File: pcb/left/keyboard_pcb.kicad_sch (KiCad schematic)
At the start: 121 parts, among them U1 Flippable RP2040 ProMicro/nic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

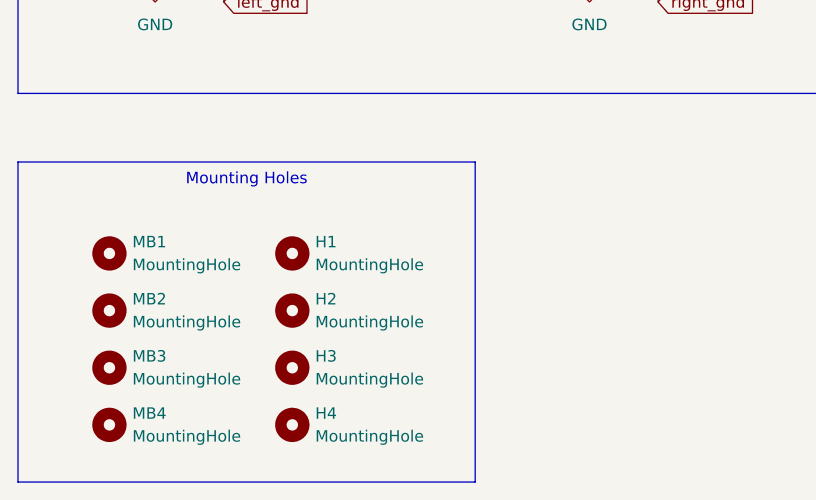
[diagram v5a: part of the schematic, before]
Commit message: Fix mounting holes
There were two H1s and three H4s! Add H5–7 and assign M2 mounting hole from KiCad library (no visible change noticed when updating on PCB).
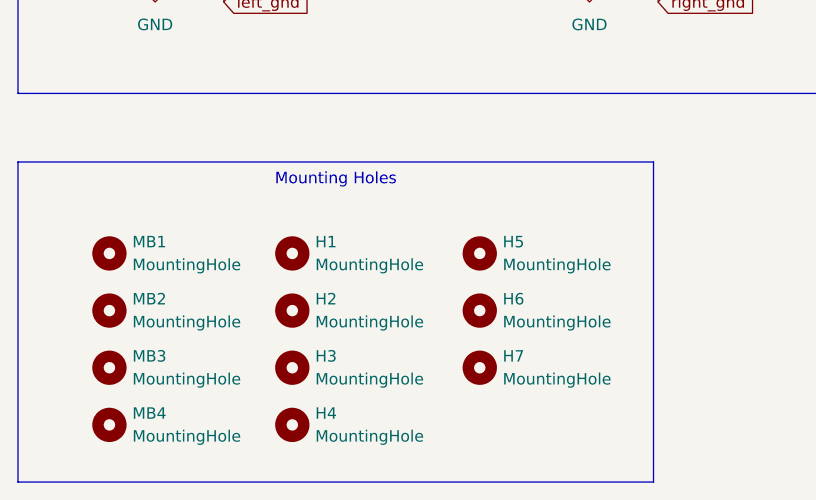
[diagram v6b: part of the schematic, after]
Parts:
- added H5, H6, H7: MountingHole, MountingHole:MountingHole_2.2mm_M2, symbol Mechanical:MountingHole
- H1, H2, H3, H4: footprint beekeeb_lib:MountingHole_2.2mm_M2-8mm -> MountingHole:MountingHole_2.2mm_M2
- 右J2, 左J2: footprint _Project Library:USB_C_Receptacle_GCT_USB4125-xx-x_6P_TopMnt_Horizontal_Flippable -> _Project Library:USB_C_Receptacle_GCT_USB4125-xx-x_6P_TopMnt_Horizontal_Mirrorable
- 右S1, 左S1: footprint _Project Library:SW_MSK12C02-HB_Flippable -> _Project Library:SW_MSK12C02-HB_Mirrorable
- 右S2: footprint _Project Library:USB_C_Receptacle_GCT_USB4125-xx-x_6P_TopMnt_Horizontal_Flippable -> (none)
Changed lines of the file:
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@@
   )
   (text_box "Mounting Holes"
-    (at 17.78 238.76 0) (size 50.8 35.56)
+    (at 17.78 238.76 0) (size 70.612 35.56)
     (stroke (width 0) (type default))
     (fill (type none))
@@
     )
   )
+  (symbol (lib_id "Mechanical:MountingHole") (at 69.088 255.27 0) (unit 1)
+    (in_bom yes) (on_board yes) (dnp no) (fields_autoplaced)
+    (property "Reference" "H6" (at 71.628 253.9999 0)
+      (effects (font (size 1.27 1.27)) (justify left))
+    )
+    (property "Value" "MountingHole" (at 71.628 256.5399 0)
+      (effects (font (size 1.27 1.27)) (justify left))
+    )
+    (property "Footprint" "MountingHole:MountingHole_2.2mm_M2" (at 69.088 255.27 0)
+      (effects (font (size 1.27 1.27)) hide)
+    )
+    (property "Datasheet" "~" (at 69.088 255.27 0)
+      (effects (font (size 1.27 1.27)) hide)
+    )
+    (instances
+      (project "keyboard_pcb"
+        (path "/9538e4ed-27e6-4c37-b989-9859dc0d49e8"
+          (reference "H6") (unit 1)
+        )
+      )
+    )
+  )
   (symbol (lib_id "Device:D") (at 269.24 229.87 90) (unit 1)
     (in_bom yes) (on_board yes) (dnp no) (fields_autoplaced)
@@
       (effects (font (size 1.27 1.27)) (justify left))
     )
-    (property "Footprint" "beekeeb_lib:MountingHole_2.2mm_M2-8mm" (at 48.26 267.97 0)
+    (property "Footprint" "MountingHole:MountingHole_2.2mm_M2" (at 48.26 267.97 0)
       (effects (font (size 1.27 1.27)) hide)
     )
@@
     )
   )
+  (symbol (lib_id "Mechanical:MountingHole") (at 69.088 261.62 0) (unit 1)
+    (in_bom yes) (on_board yes) (dnp no) (fields_autoplaced)
+    (property "Reference" "H7" (at 71.628 260.3499 0)
+      (effects (font (size 1.27 1.27)) (justify left))
+    )
+    (property "Value" "MountingHole" (at 71.628 262.8899 0)
+      (effects (font (size 1.27 1.27)) (justify left))
+    )
+    (property "Footprint" "MountingHole:MountingHole_2.2mm_M2" (at 69.088 261.62 0)
+      (effects (font (size 1.27 1.27)) hide)
+    )
+    (property "Datasheet" "~" (at 69.088 261.62 0)
+      (effects (font (size 1.27 1.27)) hide)
+    )
+    (instances
+      (project "keyboard_pcb"
+        (path "/9538e4ed-27e6-4c37-b989-9859dc0d49e8"
+          (reference "H7") (unit 1)
+        )
+      )
+    )
+  )
   (symbol (lib_id "Device:D") (at 223.52 176.53 90) (unit 1)
     (in_bom yes) (on_board yes) (dnp no) (fields_autoplaced)
@@
       (effects (font (size 1.27 1.27)) (justify left))
     )
-    (property "Footprint" "beekeeb_lib:MountingHole_2.2mm_M2-8mm" (at 48.26 255.27 0)
+    (property "Footprint" "MountingHole:MountingHole_2.2mm_M2" (at 48.26 255.27 0)
       (effects (font (size 1.27 1.27)) hide)
     )
@@
     )
   )
+  (symbol (lib_id "Mechanical:MountingHole") (at 69.088 248.92 0) (unit 1)
+    (in_bom yes) (on_board yes) (dnp no) (fields_autoplaced)
+    (property "Reference" "H5" (at 71.628 247.6499 0)
+      (effects (font (size 1.27 1.27)) (justify left))
+    )
+    (property "Value" "MountingHole" (at 71.628 250.1899 0)
+      (effects (font (size 1.27 1.27)) (justify left))
+    )
+    (property "Footprint" "MountingHole:MountingHole_2.2mm_M2" (at 69.088 248.92 0)
+      (effects (font (size 1.27 1.27)) hide)
+    )
+    (property "Datasheet" "~" (at 69.088 248.92 0)
+      (effects (font (size 1.27 1.27)) hide)
+    )
+    (instances
+      (project "keyboard_pcb"
+        (path "/9538e4ed-27e6-4c37-b989-9859dc0d49e8"
+          (reference "H5") (unit 1)
+        )
+      )
+    )
+  )
   (symbol (lib_id "Device:D") (at 190.5 250.19 90) (unit 1)
     (in_bom yes) (on_board yes) (dnp no)
@@
       (effects (font (size 1.27 1.27)))
     )
-    (property "Footprint" "_Project Library:SW_MSK12C02-HB_Flippable" (at 48.26 114.3 0)
+    (property "Footprint" "_Project Library:SW_MSK12C02-HB_Mirrorable" (at 48.26 114.3 0)
       (effects (font (size 1.27 1.27)) hide)
     )
@@
       (effects (font (size 1.27 1.27)))
     )
-    (property "Footprint" "_Project Library:SW_MSK12C02-HB_Flippable" (at 48.26 101.6 0)
+    (property "Footprint" "_Project Library:SW_MSK12C02-HB_Mirrorable" (at 48.26 101.6 0)
       (effects (font (size 1.27 1.27)) hide)
     )
@@
       (effects (font (size 1.27 1.27)))
     )
-    (property "Footprint" "_Project Library:USB_C_Receptacle_GCT_USB4125-xx-x_6P_TopMnt_Horizontal_Flippable" (at 92.71 198.12 0)
+    (property "Footprint" "_Project Library:USB_C_Receptacle_GCT_USB4125-xx-x_6P_TopMnt_Horizontal_Mirrorable" (at 92.71 198.12 0)
       (effects (font (size 1.27 1.27)) hide)
     )
@@
       (effects (font (size 1.27 1.27)) (justify left))
     )
-    (property "Footprint" "beekeeb_lib:MountingHole_2.2mm_M2-8mm" (at 48.26 261.62 0)
+    (property "Footprint" "MountingHole:MountingHole_2.2mm_M2" (at 48.26 261.62 0)
       (effects (font (size 1.27 1.27)) hide)
     )
@@
       (effects (font (size 1.27 1.27)))
     )
-    (property "Footprint" "_Project Library:USB_C_Receptacle_GCT_USB4125-xx-x_6P_TopMnt_Horizontal_Flippable" (at 44.45 198.12 0)
+    (property "Footprint" "_Project Library:USB_C_Receptacle_GCT_USB4125-xx-x_6P_TopMnt_Horizontal_Mirrorable" (at 44.45 198.12 0)
       (effects (font (size 1.27 1.27)) hide)
     )
@@
       (effects (font (size 1.27 1.27)) (justify left))
     )
-    (property "Footprint" "beekeeb_lib:MountingHole_2.2mm_M2-8mm" (at 48.26 248.92 0)
+    (property "Footprint" "MountingHole:MountingHole_2.2mm_M2" (at 48.26 248.92 0)
       (effects (font (size 1.27 1.27)) hide)
     )
@@
       (effects (font (size 1.27 1.27)))
     )
-    (property "Footprint" "_Project Library:USB_C_Receptacle_GCT_USB4125-xx-x_6P_TopMnt_Horizontal_Flippable" (at 45.72 152.4 0)
+    (property "Footprint" "" (at 45.72 152.4 0)
       (effects (font (size 1.27 1.27)) hide)
     )

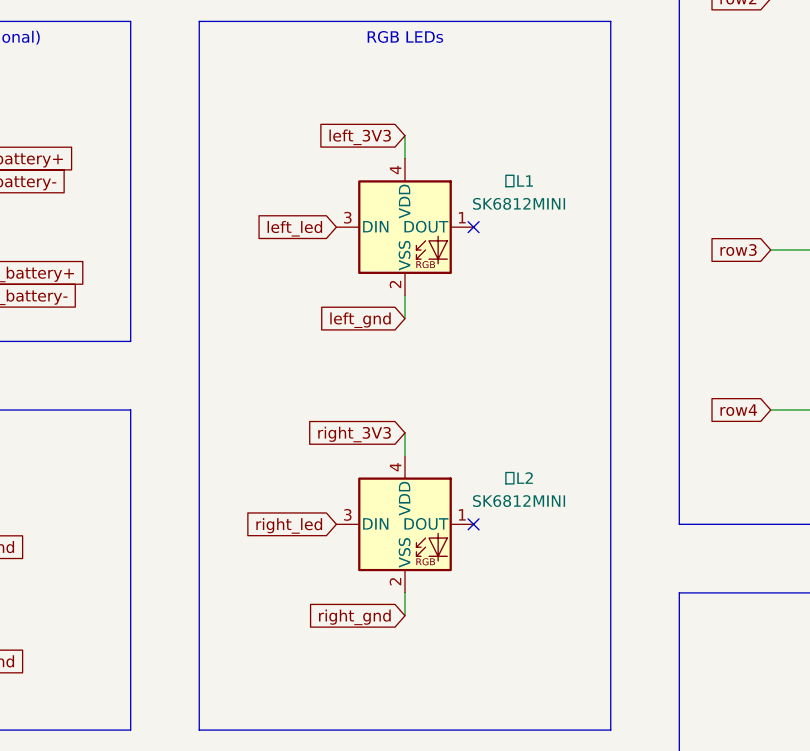
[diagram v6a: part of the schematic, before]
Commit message: Fix pin numbering for SK6812MINI-E
The “E” has a different [pinout](https://cdn-shop.adafruit.com/product-files/4960/4960_SK6812MINI-E_REV02_EN.pdf) to the non-“E”
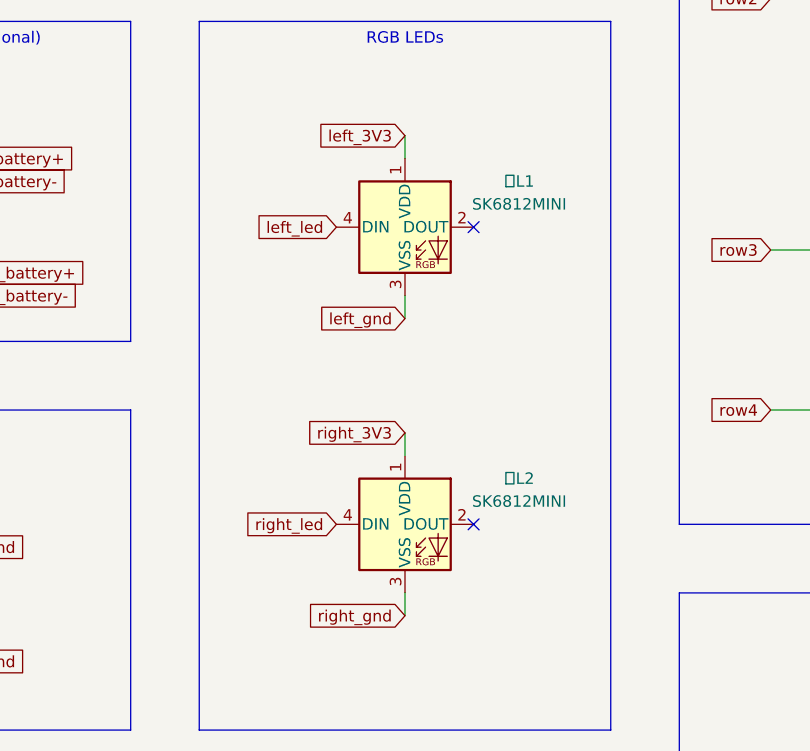
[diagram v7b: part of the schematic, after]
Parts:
- 右L2, 左L1: symbol LED:SK6812MINI -> _Project Library:SK6812MINI-E
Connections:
- net left_3V3: now also 右L2.3 (VSS), 左L1.1 (VDD); no longer 右L2.2 (VSS), 左L1.4 (VDD)
- net left_gnd: now also 右L2.1 (VDD), 左L1.3 (VSS); no longer 右L2.4 (VDD), 左L1.2 (VSS)
- net left_led: now also 左L1.4 (DIN); no longer 左L1.3 (DIN)
- net right_led: now also 右L2.4 (DIN); no longer 右L2.3 (DIN)
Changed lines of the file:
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@@
     )
   )
-  (symbol (lib_id "LED:SK6812MINI") (at 104.14 142.24 0) (unit 1)
+  (symbol (lib_id "_Project Library:SK6812MINI-E") (at 104.14 142.24 0) (unit 1)
     (in_bom yes) (on_board yes) (dnp no)
     (property "Reference" "右L2" (at 116.84 137.16 0)
@@
     )
   )
-  (symbol (lib_id "LED:SK6812MINI") (at 104.14 109.22 0) (unit 1)
+  (symbol (lib_id "_Project Library:SK6812MINI-E") (at 104.14 109.22 0) (unit 1)
     (in_bom yes) (on_board yes) (dnp no)
     (property "Reference" "左L1" (at 116.84 104.14 0)

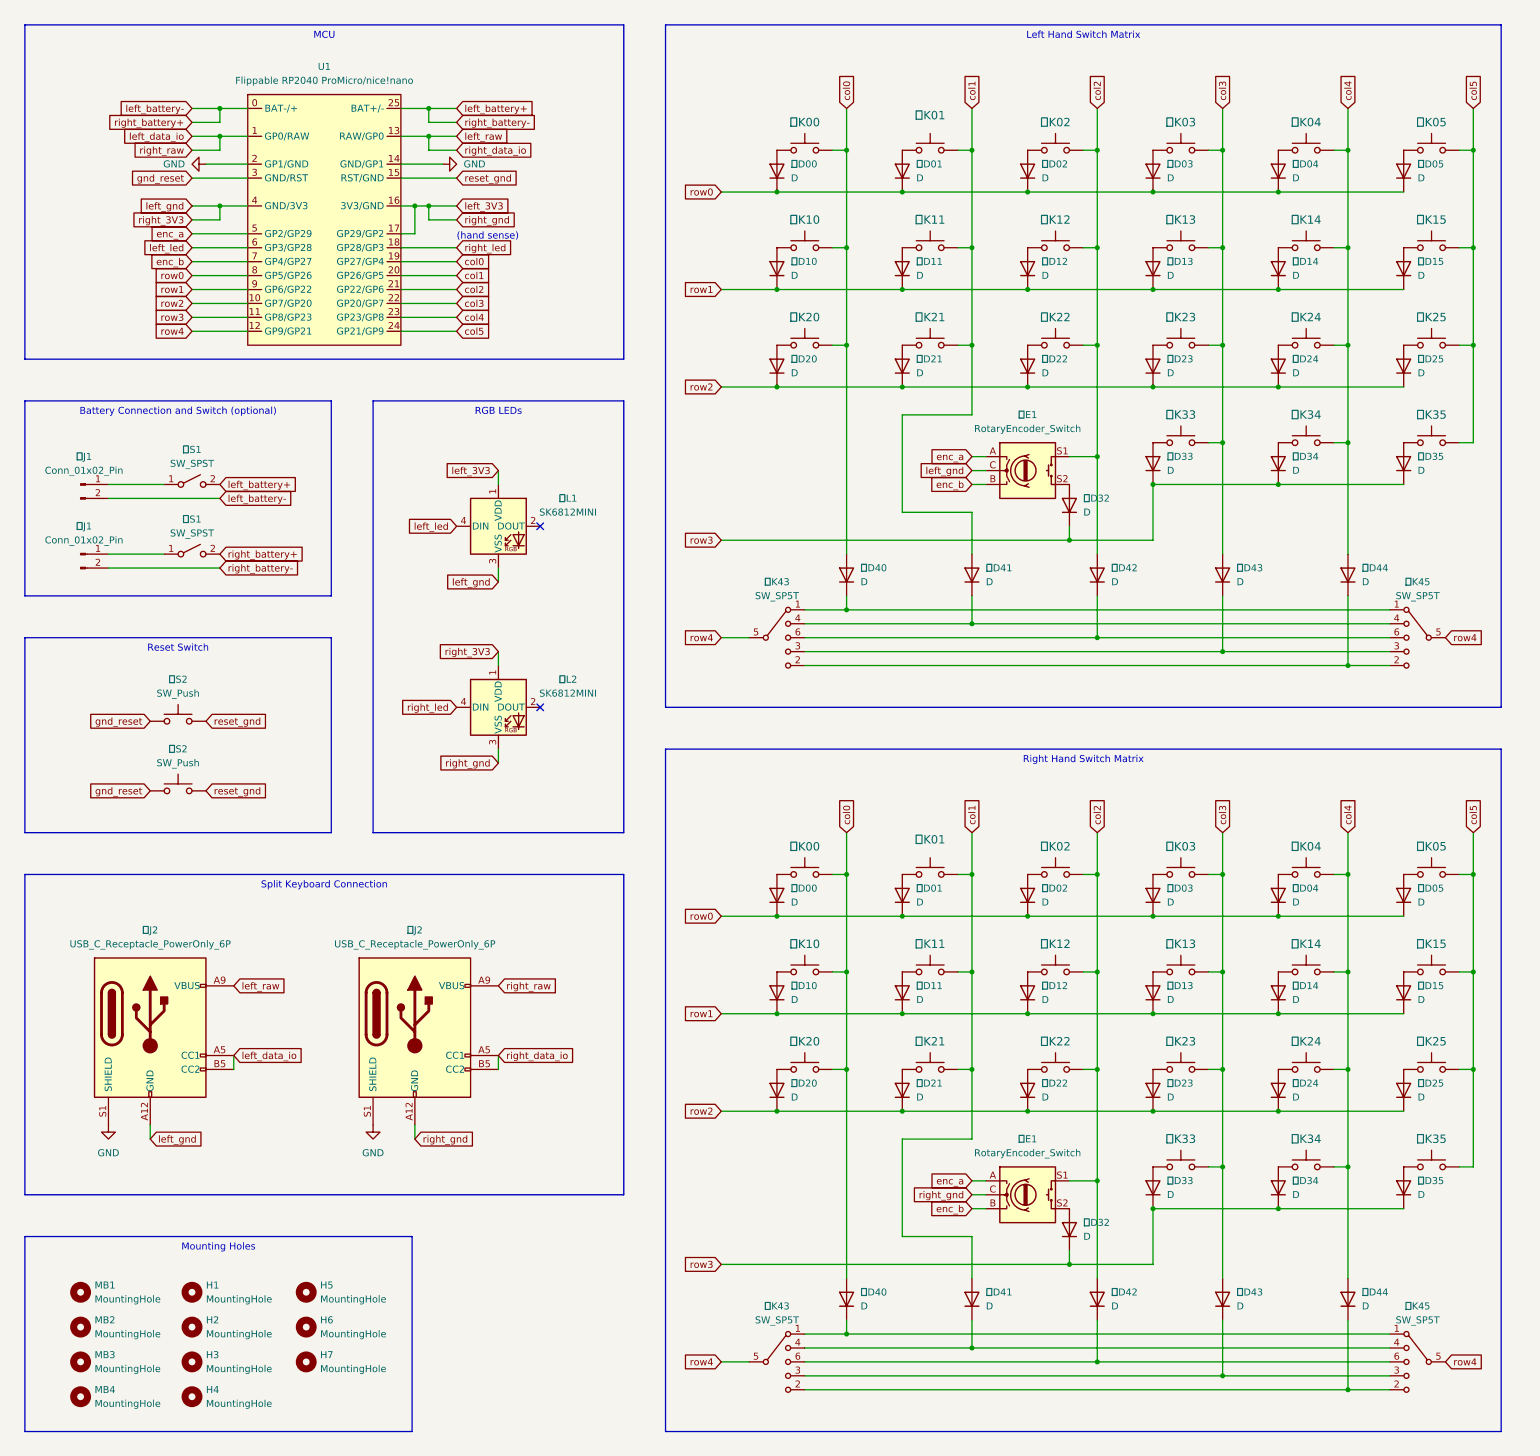
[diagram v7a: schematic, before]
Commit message: Tweak schematic
 * Change power switches to SP**D**T to match MSK12C02
 * Switch from double-named nets to single name that covers both orientations
 * Update flippable ProMicro symbol to remove gaps between pins that are no longer needed
 * Wire connection to ground through SK6812 GND leg, which will act as a jumper
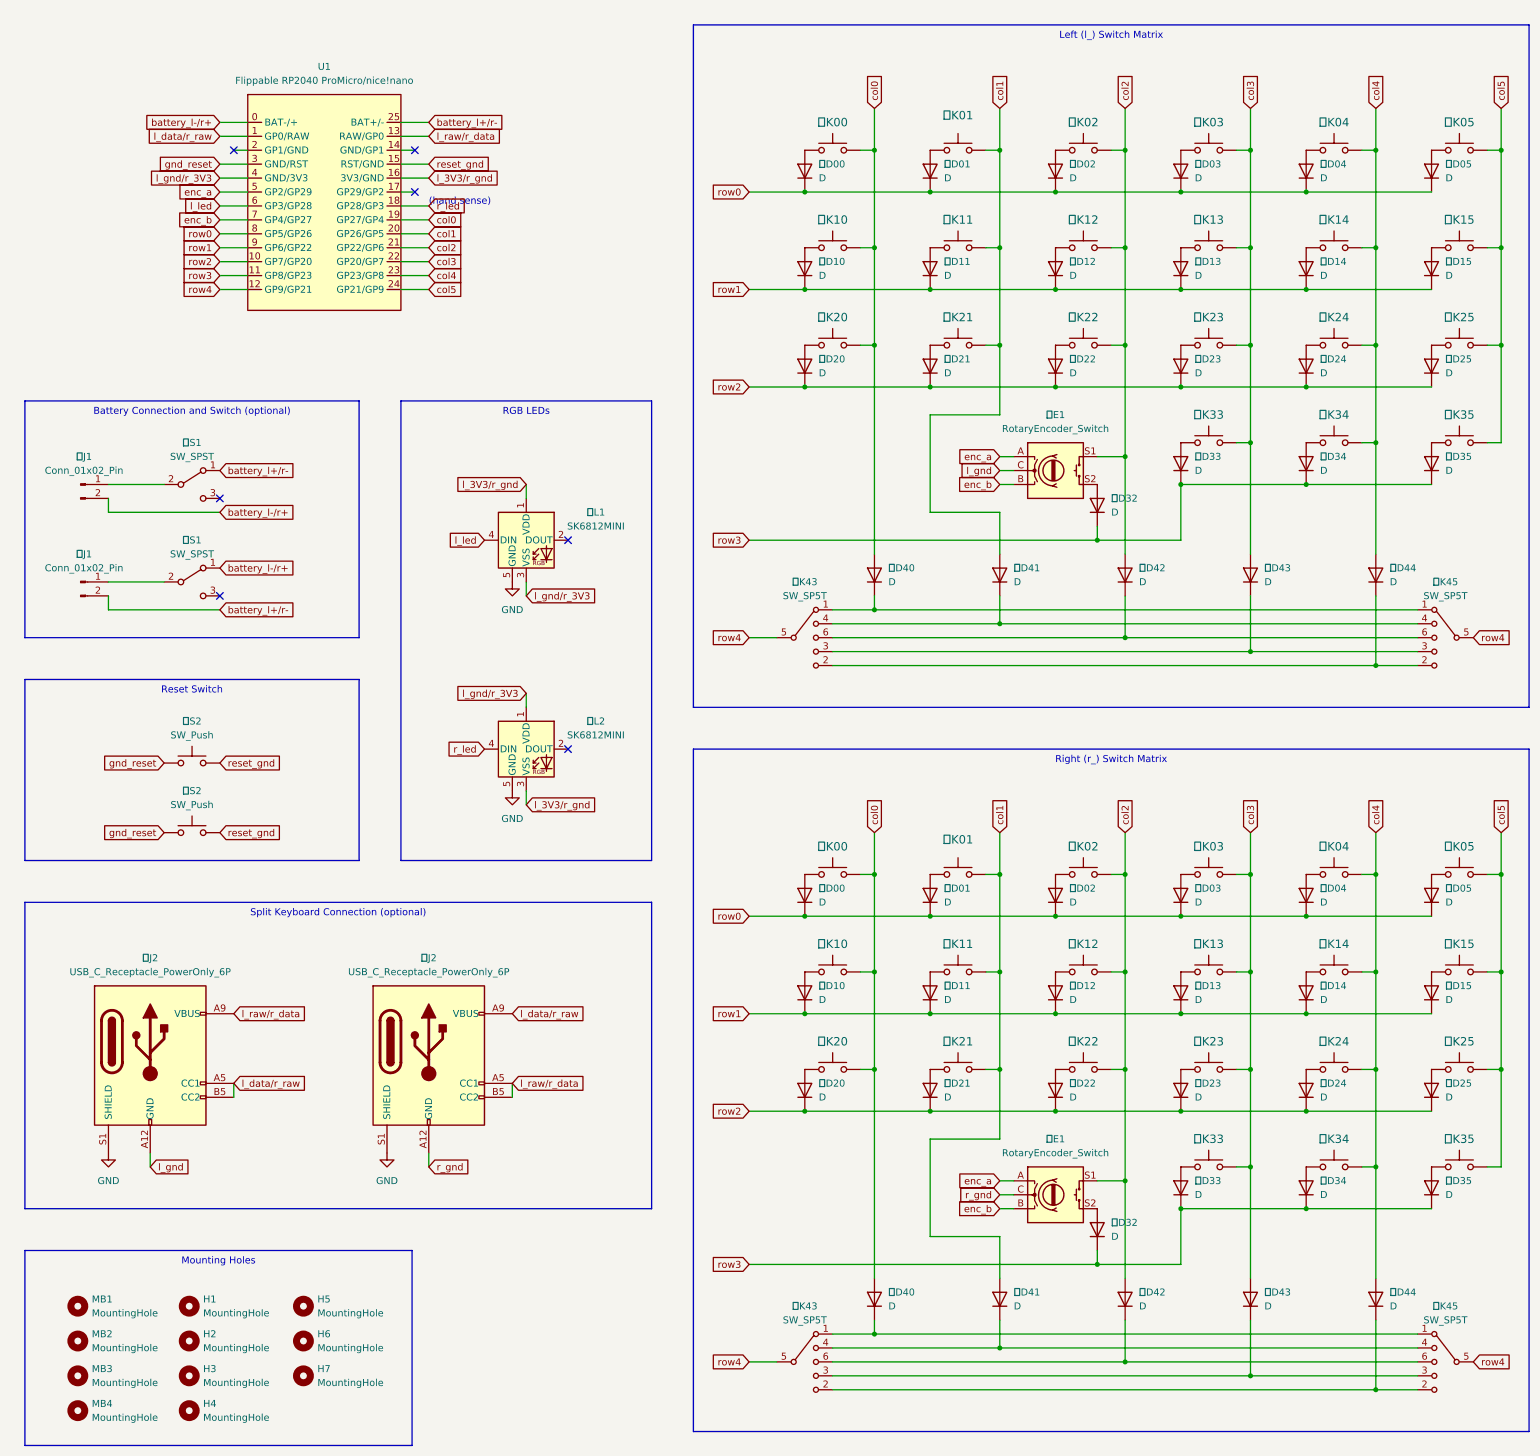
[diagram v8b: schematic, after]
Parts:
- U1: footprint (none) -> PCM_marbastlib-xp-promicroish:ProMicro_USBup
- 右L2, 左L1: footprint beekeeb_lib:SK6812-MINI-E -> _Project Library:SK6812-MINI-E_Jumped_GND
- 右S1, 左S1: symbol Switch:SW_SPST -> Switch:SW_SPDT
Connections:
- net GND: now also 右L2.5 (GND), 左L1.5 (GND); no longer U1.14 (GND/GP1), U1.2 (GP1/GND)
- net at 左J1.1 (Pin_1): now also 左S1.2 (B); no longer 左S1.1 (A)
- net at 右J1.1 (Pin_1): now also 右S1.2 (B); no longer 右S1.1 (A)
- removed net left_3V3: U1.16 (3V3/GND), U1.17 (GP29/GP2), 右E1.C, 右J2.A12 (GND), 右J2.B12 (GND), 右L2.3 (VSS), 左L1.1 (VDD)
- net left_battery+ renamed battery_l+/r-
- net battery_l+/r-: now also 左S1.1 (A); no longer 左S1.2 (B)
- net left_battery- renamed battery_l-/r+
- net battery_l-/r+: now also 右S1.1 (A); no longer 右S1.2 (B)
- net left_data_io renamed l_data/r_raw
- net left_gnd renamed l_gnd
- net l_gnd: no longer U1.4 (GND/3V3), 右L2.1 (VDD), 左L1.3 (VSS)
- net left_led renamed l_led
- net left_raw renamed l_raw/r_data
- net right_led renamed r_led
- new net l_3V3/r_gnd: U1.16 (3V3/GND), 右L2.3 (VSS), 左L1.1 (VDD)
- new net l_gnd/r_3V3: U1.4 (GND/3V3), 右L2.1 (VDD), 左L1.3 (VSS)
- new net r_gnd: 右E1.C, 右J2.A12 (GND), 右J2.B12 (GND)
- no-connect marks 2 -> 7
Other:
- moved on the sheet: H1, H2, H3, H4, H5, H6, H7, MB1, MB2, MB3, MB4, U1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
